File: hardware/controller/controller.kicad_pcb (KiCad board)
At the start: 2 copper layers, 94 parts, among them J1 USB_B_Micro, J2 Conn_01x12_Female, J3 Cooling fan, U1 DS3231MZ, U10 IS31LT3360, U2 LMR16006YQ5, U3 ESP32-WROOM, U4 LMR16006YQ5, U5 CP2102N-A01-GQFN24, U6 IS31LT3360, U7 IS31LT3360, U8 IS31LT3360, U9 IS31LT3360

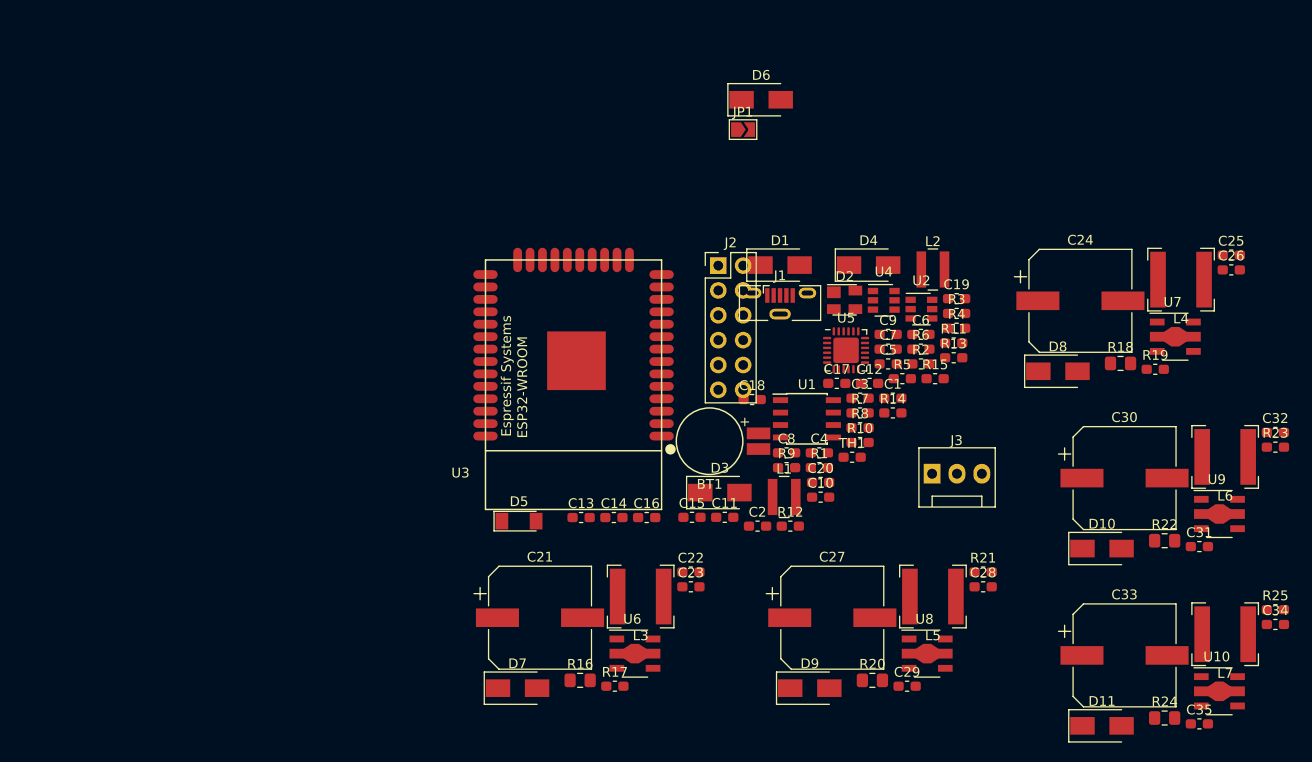
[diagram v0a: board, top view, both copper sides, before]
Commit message: initial controller components placement
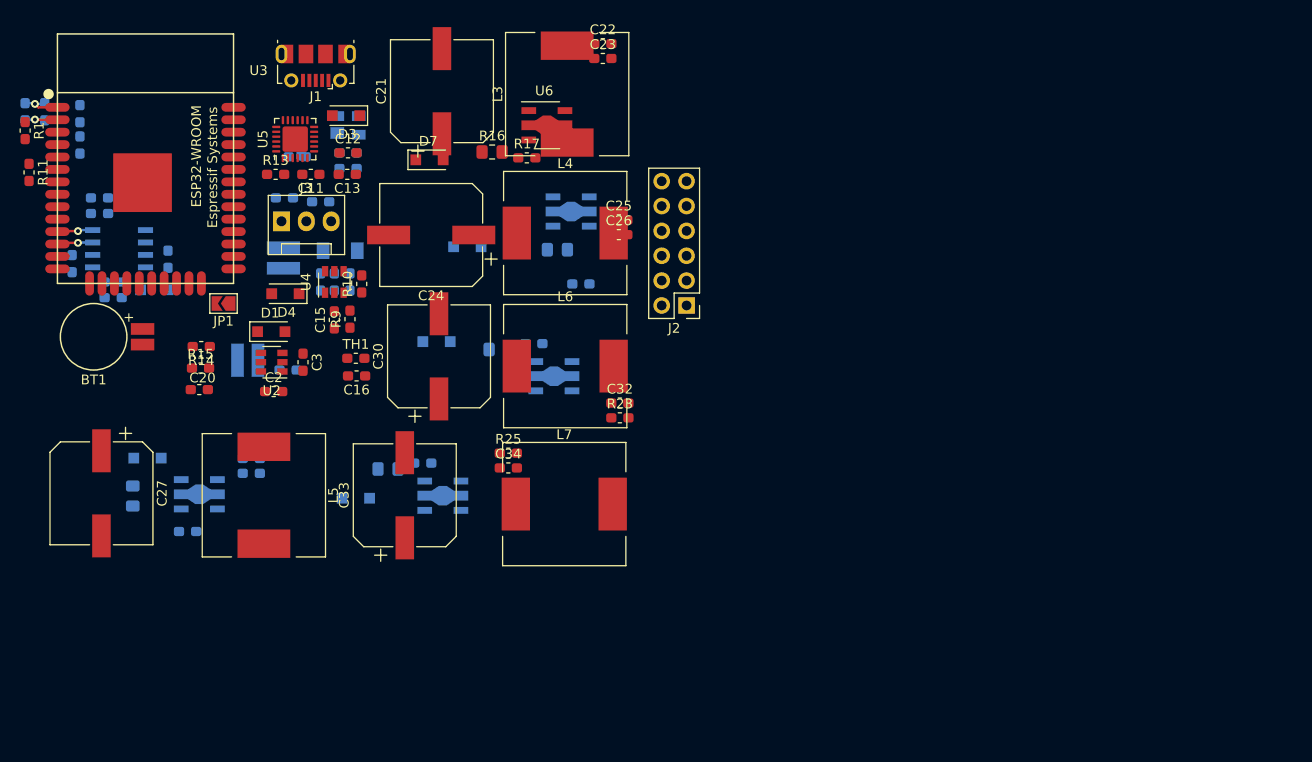
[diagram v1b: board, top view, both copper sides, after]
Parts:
- C1, C10, C14, C17, C18, C19, C28, C29, C31, C35, C4, C5, C6, C7, C8, C9, D2, D5, R12, R19, R2, R21, R3, R4, R5, R6, R7, R8, U1, U10, U7, U8, U9: moved to B.Cu
- D1, D3, D4, D7: value STPS130A -> SS14FL; footprint Diode_SMD:D_SMA -> Diode_SMD:D_SOD-123F
- D10, D11, D6, D8, D9: value STPS130A -> SS14FL; footprint Diode_SMD:D_SMA -> Diode_SMD:D_SOD-123F; moved to B.Cu
- J1: footprint Connector_USB:USB_Micro-B_Molex-105133-0001 -> led:USB_Micro-B_Molex-105017-0001
- J2: value Conn_01x12_Female -> header 2x6
- L1, L2: footprint Inductor_SMD:L_Wuerth_MAPI-4030 -> Inductor_SMD:L_Wuerth_MAPI-3015; moved to B.Cu
- L3, L4, L5, L6, L7: footprint Inductor_SMD:L_Bourns-SRN6028 -> led:L_12x12mm_H6mm
- R10: value 10k -> 1k
- R16: value 0.15 -> 0.11
- R18, R20, R22, R24: value 0.15 -> 0.11; moved to B.Cu
- R9: value 10k -> 15k
- TH1: value Thermistor -> NTCS0603E3103
- U2: value LMR16006YQ5 -> LMR16006YQ3
- U4: value LMR16006YQ5 -> LMR16006YQ
- moved R11 96.1 mm to (49.2, 78.8), turned to 270 degrees
- moved C6 94.3 mm to (48.8, 72.6), turned to 270 degrees
- moved C19 91.0 mm to (54.4, 76.0), turned to 270 degrees
- moved C5 90.0 mm to (50.8, 72.6), turned to 90 degrees
- moved R3 88.4 mm to (56.4, 81.4)
- moved R4 88.4 mm to (56.4, 83.0)
- moved R1 88.2 mm to (48.8, 74.5), turned to 270 degrees
- moved C35 83.7 mm to (89.4, 108.5)
- moved R24 83.4 mm to (85.9, 109.1)
- moved C4 83.1 mm to (54.4, 72.8), turned to 270 degrees
- moved U10 81.9 mm to (91.5, 111.8)
- moved C34 80.0 mm to (98.2, 109.0)
- moved R25 80.0 mm to (98.2, 107.5)
- moved D11 79.7 mm to (82.6, 112.1)
- moved C7 79.5 mm to (57.8, 90.0)
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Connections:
- C18 pad 2: (no net) -> FAN_PWR
- U3 pad 11: (no net) -> i2c_scl
- U3 pad 12: (no net) -> i2c_sda
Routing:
- net GND: track 0.00 -> 4.51 mm, vias 0 -> 1
- net +3V3: track 0.00 -> 4.37 mm, vias 0 -> 1
- net i2c_sda: track 0.00 -> 3.66 mm, vias 0 -> 1
- net i2c_scl: track 0.00 -> 3.66 mm, vias 0 -> 1

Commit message: controller partially traced
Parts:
- added J4: Input power, Connector:FanPinHeader_1x03_P2.54mm_Vertical, F.Cu at (116.0, 78.8)
- added REF**: KiCad-Logo2_6mm_SilkScreen, Symbol:KiCad-Logo2_6mm_SilkScreen, F.Cu at (116.2, 87.0)
- added REF**: OSHW-Logo_5.7x6mm_SilkScreen, Symbol:OSHW-Logo_5.7x6mm_SilkScreen, F.Cu at (131.8, 96.9)
- added REF**: MountingHole_3.2mm_M3, MountingHole:MountingHole_3.2mm_M3, F.Cu at (54.0, 120.0)
- added REF**: MountingHole_3.2mm_M3, MountingHole:MountingHole_3.2mm_M3, F.Cu at (116.0, 120.0)
- added REF**: MountingHole_3.2mm_M3, MountingHole:MountingHole_3.2mm_M3, F.Cu at (116.0, 68.0)
- added REF**: MountingHole_3.2mm_M3, MountingHole:MountingHole_3.2mm_M3, F.Cu at (54.0, 68.0)
- C19: moved to F.Cu
- C2, C22, C23, C25, C26, C32, C34, D7, R1, R11, R16, R17, R23, R25, U6: moved to B.Cu
- moved J1 40.4 mm to (54.0, 100.0), turned to 270 degrees
- moved C20 28.5 mm to (53.2, 75.9), turned to 270 degrees
- moved C11 27.3 mm to (60.4, 99.9), turned to 0 degrees
- moved R13 27.1 mm to (66.0, 104.8), turned to 90 degrees
- moved C12 26.4 mm to (65.8, 97.8)
- moved C13 26.4 mm to (65.7, 100.0)
- moved D2 26.4 mm to (65.8, 95.0)
- moved D3 26.4 mm to (65.6, 94.0)
- moved R7 26.4 mm to (65.8, 97.8)
- moved R8 26.4 mm to (65.8, 99.4)
- moved U5 26.4 mm to (60.4, 96.4), turned to 0 degrees
- moved C10 26.4 mm to (60.6, 98.2)
- moved R6 26.2 mm to (60.5, 96.5), turned to 180 degrees
- moved R15 22.5 mm to (53.2, 80.8), turned to 270 degrees
- moved J3 20.4 mm to (69.0, 103.2)
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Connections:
- C23 pad 1: Net-(C23-Pad1) -> LED1+
- C26 pad 1: Net-(C26-Pad1) -> LED2+
- C29 pad 1: Net-(C29-Pad1) -> LED3+
- C32 pad 1: Net-(C32-Pad1) -> LED4+
- C35 pad 1: Net-(C35-Pad1) -> LED5+
- J2 pad 1: (no net) -> LED1+
- J2 pad 3: (no net) -> LED2+
- J2 pad 5: (no net) -> LED3+
- J2 pad 7: (no net) -> LED4+
- J2 pad 9: (no net) -> LED5+
- R16 pad 1: Net-(C23-Pad1) -> LED1+
- R18 pad 1: Net-(C26-Pad1) -> LED2+
- R20 pad 1: Net-(C29-Pad1) -> LED3+
- R22 pad 1: Net-(C32-Pad1) -> LED4+
- R24 pad 1: Net-(C35-Pad1) -> LED5+
- U10 pad 4: Net-(C35-Pad1) -> LED5+
- U6 pad 4: Net-(C23-Pad1) -> LED1+
- U7 pad 4: Net-(C26-Pad1) -> LED2+
- U8 pad 4: Net-(C29-Pad1) -> LED3+
- U9 pad 4: Net-(C32-Pad1) -> LED4+
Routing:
- net GND: track 4.51 -> 293.5 mm, vias 1 -> 6
- net VDD: track 0.00 -> 143.8 mm, vias 0 -> 2
- net LED3-: track 0.00 -> 72.6 mm, vias 0 -> 4
- net LED_ADJ_1: track 0.00 -> 52.2 mm, vias 0 -> 1
- net LED1-: track 0.00 -> 45.3 mm, vias 0 -> 3
- net LED4-: track 0.00 -> 40.4 mm
- net LED1+: track 0.00 -> 37.1 mm, vias 0 -> 1
- net LED2+: track 0.00 -> 35.7 mm, vias 0 -> 2
- net +3V3: track 4.37 -> 39.0 mm, vias 1 -> 3
- net LED5-: track 0.00 -> 28.6 mm, vias 0 -> 1
- net LED2-: track 0.00 -> 26.4 mm, vias 0 -> 2
- net Net-(C12-Pad2): track 0.00 -> 23.7 mm, vias 0 -> 1
- net Net-(BT1-Pad1): track 0.00 -> 18.5 mm, vias 0 -> 1
- net Net-(D2-Pad2): track 0.00 -> 15.9 mm, vias 0 -> 2
- net Net-(D7-Pad2): track 0.00 -> 12.9 mm, vias 0 -> 1
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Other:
- board outline added: 70 x 60 mm
- board text added: "Licensed under CERN OHL v.1.2"

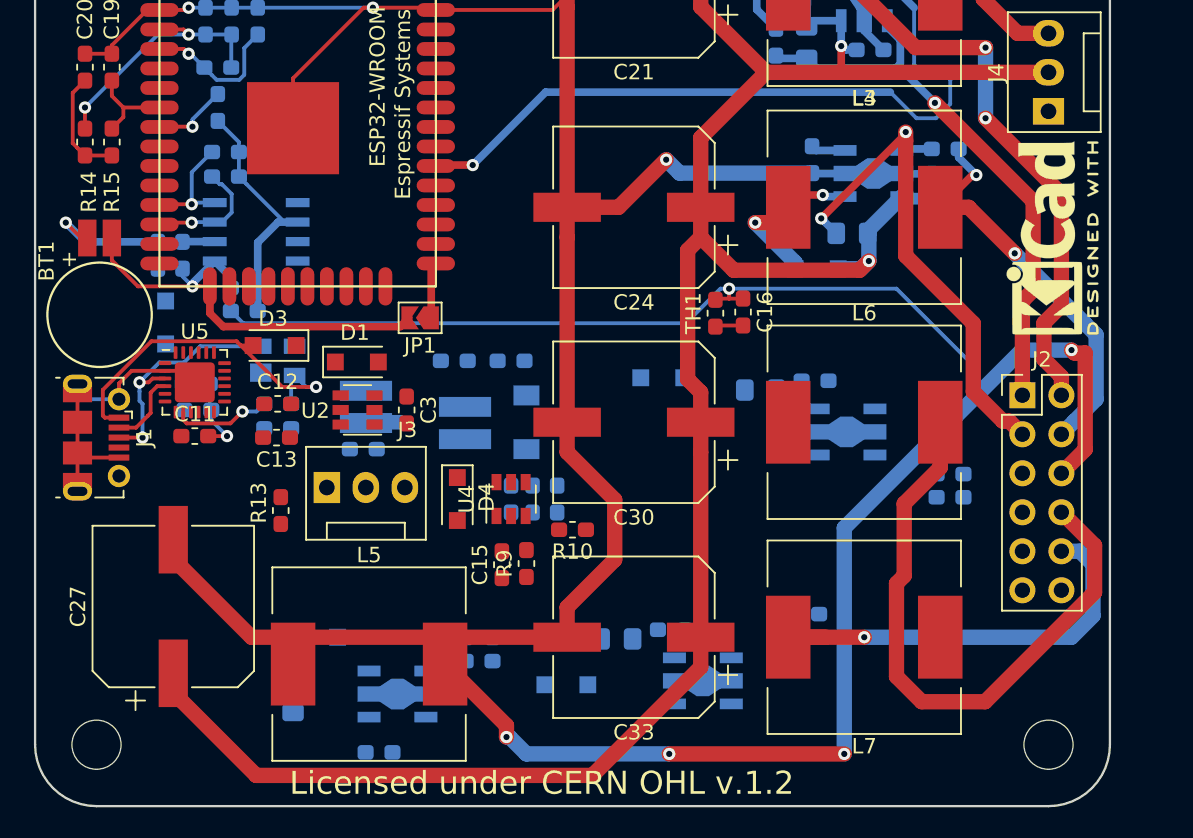
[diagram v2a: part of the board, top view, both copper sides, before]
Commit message: led array rework for fr4 board
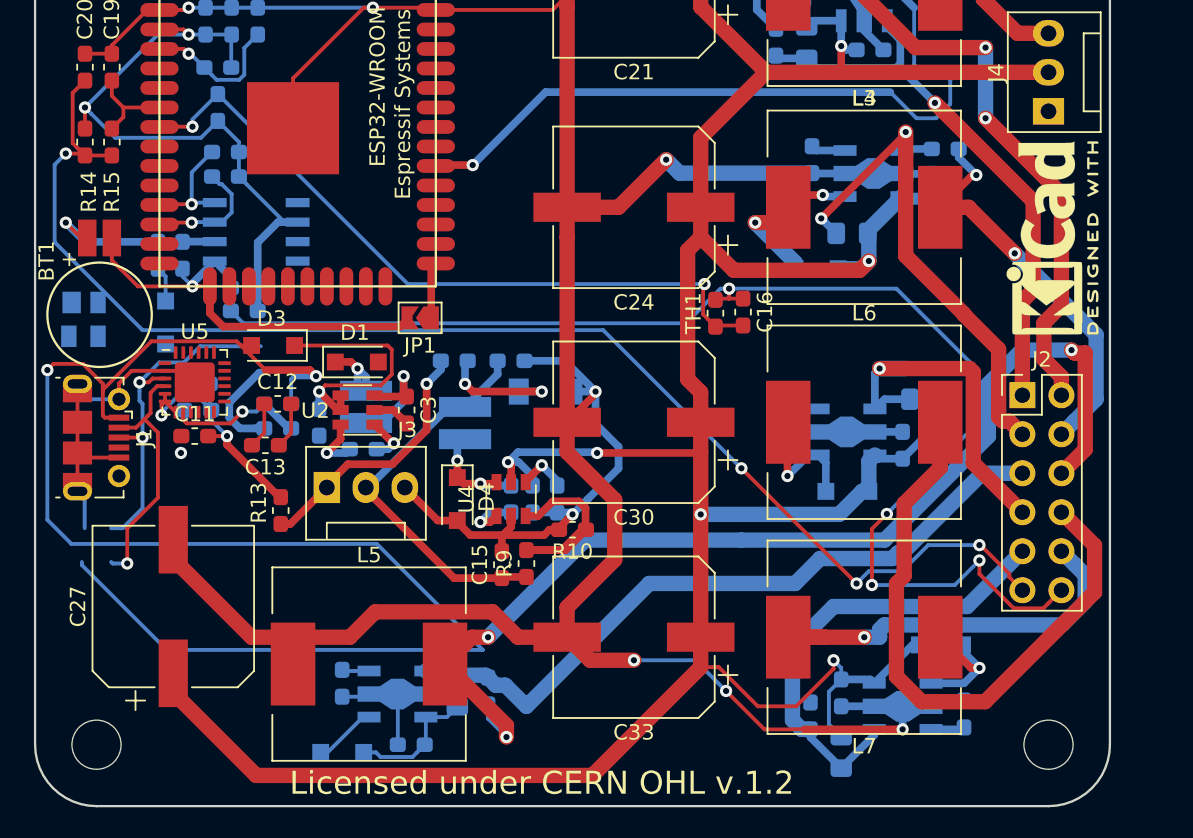
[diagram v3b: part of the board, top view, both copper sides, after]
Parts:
- moved D11 24.5 mm to (109.0, 113.5)
- moved R24 16.4 mm to (102.5, 120.5), turned to 90 degrees
- moved D10 14.1 mm to (102.9, 103.5), turned to 180 degrees
- moved U10 13.1 mm to (106.5, 117.5), turned to 180 degrees
- moved D2 12.9 mm to (53.1, 92.3), turned to 270 degrees
- moved R25 12.2 mm to (110.5, 118.0), turned to 90 degrees
- moved R23 11.8 mm to (99.0, 98.6), turned to 270 degrees
- moved R22 10.8 mm to (108.0, 97.5)
- moved R20 10.7 mm to (77.5, 116.5), turned to 270 degrees
- moved C35 10.7 mm to (100.5, 118.1), turned to 90 degrees
- moved R21 9.39 mm to (70.0, 116.0), turned to 270 degrees
- moved C29 8.15 mm to (79.5, 116.5), turned to 270 degrees
- moved D9 7.69 mm to (70.0, 120.5), turned to 180 degrees
- moved C32 7.15 mm to (107.6, 95.5)
- moved C31 7.08 mm to (106.5, 100.5), turned to 90 degrees
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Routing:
- net GND: track 293.5 -> 419.5 mm, vias 6 -> 15
- net VDD: track 143.8 -> 230.7 mm, vias 2 -> 7
- net Net-(C20-Pad2): track 7.29 -> 89.3 mm, vias 0 -> 4
- net Net-(C12-Pad2): track 23.7 -> 101.2 mm, vias 1 -> 2
- net LED3+: track 0.00 -> 46.1 mm
- net Net-(C16-Pad2): track 6.80 -> 46.8 mm, vias 1 -> 2
- net LED5+: track 0.00 -> 30.5 mm
- net +3V3: track 39.0 -> 69.3 mm, vias 3 -> 5
- net FAN_PWR: track 0.00 -> 25.5 mm
- net LED4+: track 0.00 -> 23.7 mm, vias 0 -> 1
- net Net-(J3-Pad1): track 0.00 -> 17.0 mm, vias 0 -> 1
- net Net-(R10-Pad1): track 0.00 -> 14.6 mm
- net Net-(D2-Pad3): track 4.90 -> 16.6 mm, vias 0 -> 1
- net Net-(D11-Pad2): track 0.00 -> 8.90 mm, vias 0 -> 1
- net Net-(D10-Pad2): track 0.00 -> 8.66 mm, vias 0 -> 1
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
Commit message: controller finished. Sent both boards for manufacturing
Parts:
- C11, U5: moved to B.Cu
- D2, L1: moved to F.Cu
- D5: value 5v1 -> BZV55C5V1
- moved REF** 74.5 mm to (61.2, 120.6), turned to 0 degrees
- moved U5 17.2 mm to (57.8, 113.4), turned to 270 degrees
- moved R6 16.0 mm to (61.2, 112.5), turned to 270 degrees
- moved D2 11.2 mm to (59.4, 101.6), turned to 90 degrees
- moved D6 10.9 mm to (55.6, 82.0), turned to 90 degrees
- moved C10 10.8 mm to (56.0, 108.0)
- moved C11 10.7 mm to (56.0, 109.6)
- moved R8 9.22 mm to (58.3, 104.8)
- moved R7 8.35 mm to (58.4, 101.7), turned to 270 degrees
- moved C13 8.22 mm to (58.4, 95.6)
- moved C12 7.42 mm to (58.4, 97.2)
- moved L1 5.95 mm to (66.0, 95.8), turned to 90 degrees
- moved D3 5.08 mm to (61.4, 97.0), turned to 90 degrees
- moved R2 3.08 mm to (55.6, 86.2), turned to 270 degrees
- moved R13 2.56 mm to (66.2, 102.2)
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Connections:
- R7 pad 2: Net-(R7-Pad2) -> usb_present
- R8 pad 1: Net-(R7-Pad2) -> usb_present
- U3 pad 24: (no net) -> usb_present
- U3 pad 28: (no net) -> 12v~SHDN
- U3 pad 9: 12v~SHDN -> (no net)
- U5 pad 8: Net-(R7-Pad2) -> usb_present
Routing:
- net GND: track 419.5 -> 526.3 mm, vias 15 -> 20
- net Net-(C12-Pad2): track 101.2 -> 13.2 mm
- net esp32_uart_tx: track 0.00 -> 70.7 mm, vias 0 -> 1
- net esp32_uart_rx: track 0.00 -> 70.5 mm, vias 0 -> 1
- net LED_ADJ_5: track 2.20 -> 72.1 mm, vias 0 -> 3
- net LED_ADJ_3: track 1.78 -> 57.6 mm, vias 0 -> 1
- net LED_ADJ_4: track 2.15 -> 46.5 mm, vias 0 -> 3
- net usb_present: track 0.00 -> 42.4 mm, vias 0 -> 1
- net +3V3: track 69.3 -> 101.9 mm, vias 5 -> 7
- net LED_ADJ_2: track 2.26 -> 32.6 mm, vias 0 -> 1
- net VDD: track 230.7 -> 252.5 mm, vias 7 -> 9
- net 12v~SHDN: track 3.34 -> 24.5 mm
- net Net-(R7-Pad2): track 8.82 -> 0.00 mm, vias 1 -> 0
- net Net-(D9-Pad2): track 4.10 -> 12.4 mm, vias 0 -> 1
- net LED5-: track 27.0 -> 34.2 mm
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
